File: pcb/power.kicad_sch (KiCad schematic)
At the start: 60 parts, among them J7 1S LiPo, Q1 Q_Dual_NMOS_S1G1S2G2D2D2D1D1, Q2 Q_Dual_NMOS_S1G1S2G2D2D2D1D1, Q3 Q_Dual_NMOS_S1G1S2G2D2D2D1D1, U13 BQ25798, U14 TPS63060, U15 TPS61089

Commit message: add the capacitor the charger's system pin was owed, and take the switch nodes off the top layer
Three things, all of them the charger's own layout list read one item at a time.

C97 is a new part in the drawing. Item one asks for a 0.1uF at the SYS pin on top of the IC, and this
board had one 0.1uF on the system rail with two parts entitled to it -- the charger's SYS pin and the
3.3V converter's input, different pins on different packages millimetres apart. One capacitor cannot
sit on top of both, and the placement pass had to choose, so the charger's was simply missing. Each
pin now has its own, at 1.6mm and 1.5mm.

The switch nodes now leave through a column of vias to the back, which is item two and follows from
item one: holding the capacitors against the package leaves the inductor nowhere near to go. The back
rather than an inner layer on purpose -- the inner layers here are a solid ground plane and the
rails, and a switch node run between them is a capacitor to both along its whole length, against the
same item's instruction to minimize parasitic capacitance from that area to any other trace or plane.
Three vias at the pin and two at the coil, per item six. It works on the buck-boost and not on the
other two: a 0.6mm via wants more room beside a pin than the charger's 0.4mm pitch leaves, and going
smaller would mean a via under the board's own minimum, which is not a trade to make quietly.

And the reservoirs follow the small capacitors in, one per part per rail, which is the rest of item
one and the whole of item five. The battery reservoir went from 14.0mm to 3.2mm and REGN from 8.7 to
2.2mm.

Four faults of my own on the way, each found by measuring rather than by reading the code. Matching a
capacitor to a pin by net alone dragged nine of the processor's and hub's decoupling to the 3.3V
converter's output; it has to be the same sheet. Claiming by PIN let one part take every capacitor on
a rail it has two pins on, so both system-rail capacitors went to th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
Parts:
- added C97: 100n, Capacitor_SMD:C_0402_1005Metric, symbol Device:C_Small
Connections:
- net GND: now also C97.2
- net VSYS: now also C97.1
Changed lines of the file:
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@@
 		(color 0 0 0 0)
 	)
+	(symbol
+		(lib_id "Device:C_Small")
+		(at 114.30 162.56 0)
+		(unit 1)
+		(body_style 1)
+		(exclude_from_sim no)
+		(in_bom yes)
+		(on_board yes)
+		(in_pos_files yes)
+		(dnp no)
+		(property "Reference" "C97"
+			(at 114.30 154.94 0)
+			(show_name no)
+			(do_not_autoplace no)
+			(effects
+				(font
+					(size 1.27 1.27)
+				)
+			)
+		)
+		(property "Value" "100n"
+			(at 114.30 170.18 0)
+			(show_name no)
+			(do_not_autoplace no)
+			(effects
+				(font
+					(size 1.27 1.27)
+				)
+			)
+		)
+		(property "Voltage" "16V"
+			(at 114.30 170.18 0)
+			(hide yes)
+			(show_name no)
+			(do_not_autoplace no)
+			(effects
+				(font
+					(size 1.27 1.27)
+				)
+			)
+		)
+		(property "Dielectric" "X7R"
+			(at 114.30 170.18 0)
+			(hide yes)
+			(show_name no)
+			(do_not_autoplace no)
+			(effects
+				(font
+					(size 1.27 1.27)
+				)
+			)
+		)
+		(property "Footprint" "Capacitor_SMD:C_0402_1005Metric"
+			(at 114.30 162.56 0)
+			(show_name no)
+			(do_not_autoplace no)
+			(effects
+				(font
+					(size 1.27 1.27)
+				)
+			)
+		)
+		(property "Datasheet" ""
+			(at 114.30 162.56 0)
+			(show_name no)
+			(do_not_autoplace no)
+			(effects
+				(font
+					(size 1.27 1.27)
+				)
+			)
+		)
+		(property "Description" ""
+			(at 114.30 162.56 0)
+			(show_name no)
+			(do_not_autoplace no)
+			(effects
+				(font
+					(size 1.27 1.27)
+				)
+			)
+		)
+		(pin "1"
+		)
+		(pin "2"
+		)
+		(instances
+			(project "crossfire"
+				(path "/4c5cdd13-4f54-43b0-affb-0ae4b9a4d279/3a0d800d-f868-47e5-a520-4703480651cc"
+					(reference "C97")
+					(unit 1)
+				)
+			)
+		)
+	)
+	(symbol
+		(lib_id "power:GND")
+		(at 114.30 170.18 0)
+		(unit 1)
+		(body_style 1)
+		(exclude_from_sim no)
+		(in_bom yes)
+		(on_board yes)
+		(in_pos_files yes)
+		(dnp no)
+		(property "Reference" "#PWR119"
+			(at 114.30 163.83 0)
+			(hide yes)
+			(show_name no)
+			(do_not_autoplace no)
+			(effects
+				(font
+					(size 1.27 1.27)
+				)
+			)
+		)
+		(property "Value" "GND"
+			(at 114.30 173.99 0)
+			(show_name no)
+			(do_not_autoplace no)
+			(effects
+				(font
+					(size 1.27 1.27)
+				)
+			)
+		)
+		(property "Footprint" ""
+			(at 114.30 170.18 0)
+			(show_name no)
+			(do_not_autoplace no)
+			(effects
+				(font
+					(size 1.27 1.27)
+				)
+			)
+		)
+		(property "Datasheet" ""
+			(at 114.30 170.18 0)
+			(show_name no)
+			(do_not_autoplace no)
+			(effects
+				(font
+					(size 1.27 1.27)
+				)
+			)
+		)
+		(property "Description" ""
+			(at 114.30 170.18 0)
+			(show_name no)
+			(do_not_autoplace no)
+			(effects
+				(font
+					(size 1.27 1.27)
+				)
+			)
+		)
+		(pin "1"
+		)
+		(instances
+			(project "crossfire"
+				(path "/4c5cdd13-4f54-43b0-affb-0ae4b9a4d279/3a0d800d-f868-47e5-a520-4703480651cc"
+					(reference "#PWR119")
+					(unit 1)
+				)
+			)
+		)
+	)
+	(wire
+		(pts
+			(xy 114.30 160.02) (xy 114.30 157.48)
+		)
+		(stroke
+			(width 0)
+			(type default)
+		)
+	)
+	(wire
+		(pts
+			(xy 114.30 165.10) (xy 114.30 170.18)
+		)
+		(stroke
+			(width 0)
+			(type default)
+		)
+	)
+	(wire
+		(pts
+			(xy 104.14 157.48) (xy 114.30 157.48)
+		)
+		(stroke
+			(width 0)
+			(type default)
+		)
+	)
+	(junction
+		(at 104.14 157.48)
+		(diameter 0)
+		(color 0 0 0 0)
+	)
 )

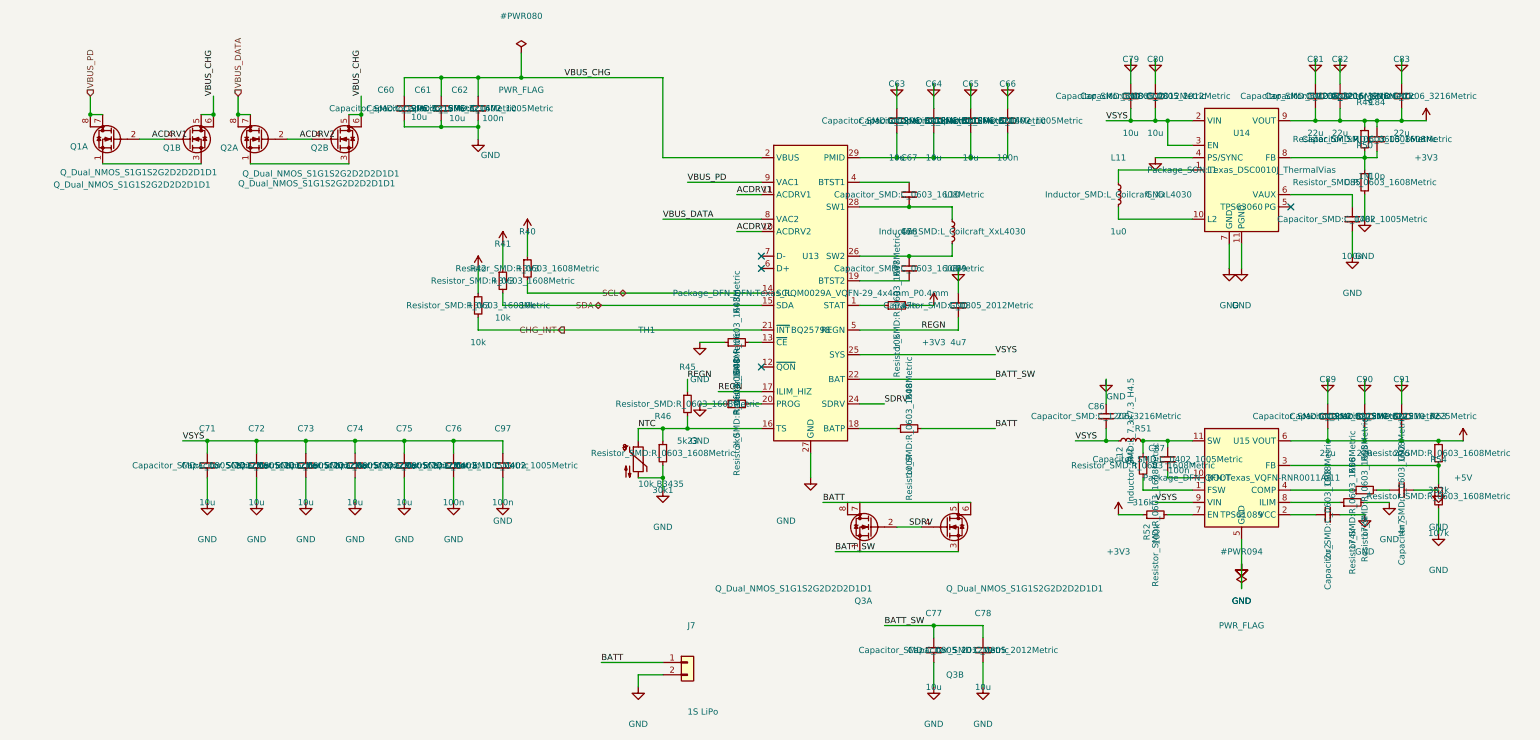
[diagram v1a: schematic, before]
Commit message: checkpoint the battery, PD and radio design as it stood
The last state of the full-featured board before it is reduced to a single
USB-C input: the power block re-placed part by part in order of importance,
the charger's signal pins fanned out, the differential pairs renamed so the
layout tool recognises them, the 3.3 V converter's feedback divider joined
to its pin, the FETs given their part number, and the non-printing fields
hidden on the schematic. The layout is incomplete and is recorded as such.

Co-Authored-By: Claude Fable 5.1 <noreply@anthropic.com>
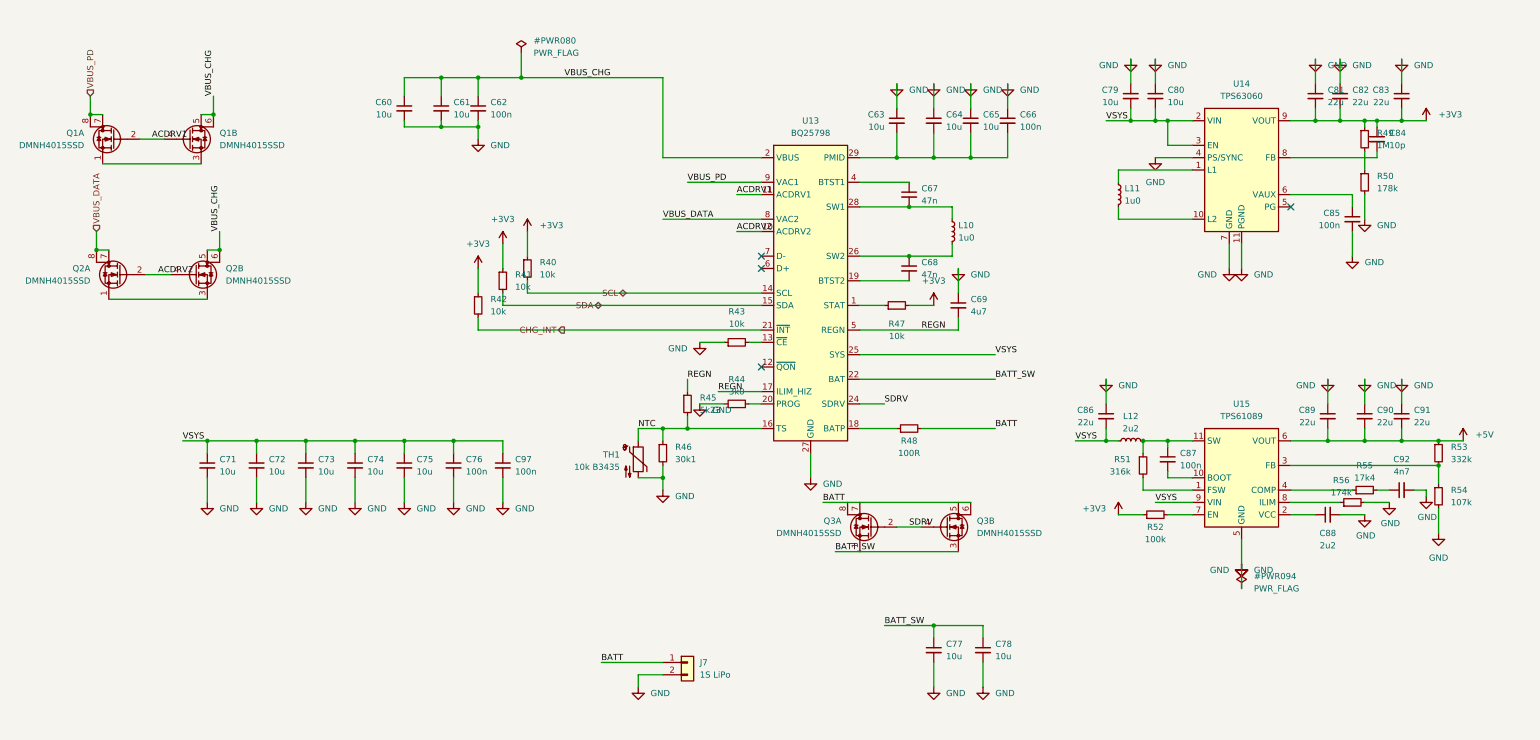
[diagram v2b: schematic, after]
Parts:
- Q1, Q2, Q3: value Q_Dual_NMOS_S1G1S2G2D2D2D1D1 -> DMNH4015SSD
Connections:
- net at R49.2, R50.1: no longer C84.2, U14.8 (FB)
- new net: C84.2, U14.8 (FB)
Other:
- moved on the sheet: Q2A, Q2B

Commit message: reduce the board to a single USB-C input
The PD sink and its connector, the charger and the cell, the input and ship
switches, the 5 V boost, the 3.3 V buck-boost and the radio come off. The
one remaining USB-C receptacle carries data to the hardware controller and
its VBUS is the 5 V rail: straight to the four port switches, and to a
fixed 3.3 V buck (AP63203) for everything else.

The two CC pins are read by ADC inputs through 10k into 100n, in series so
the 5.1k termination is not loaded, so firmware can tell a 3 A source from
a 1.5 A one from a default port and power the ports to fit.

Schematic: radio and upstream_power sheets removed, power sheet redrawn,
seven MCU pins freed and two taken. Board: 61 footprints and 514 tracks and
vias removed, survivors re-netted from the netlist, new parts loaded but
not placed. The layout is to be redone and the design document says so; it
is rewritten for this design, with what the single input gives up stated.

Co-Authored-By: Claude Fable 5.1 <noreply@anthropic.com>
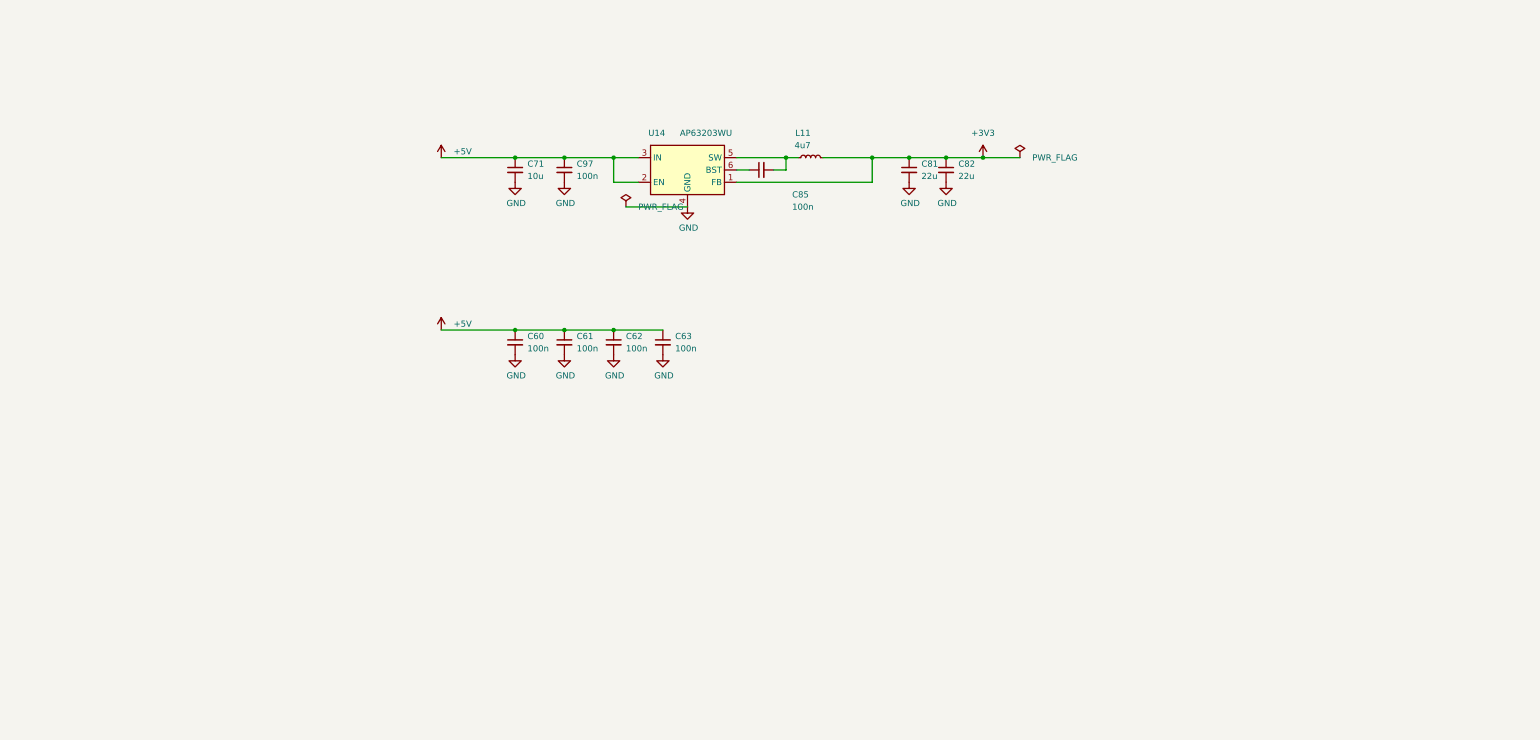
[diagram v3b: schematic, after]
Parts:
- removed C64, C65: 10u, Capacitor_SMD:C_1206_3216Metric, symbol Device:C_Small
- removed C66, C76, C87: 100n, Capacitor_SMD:C_0402_1005Metric, symbol Device:C_Small
- removed C67, C68: 47n, Capacitor_SMD:C_0603_1608Metric, symbol Device:C_Small
- removed C69: 4u7, Capacitor_SMD:C_0805_2012Metric, symbol Device:C_Small
- removed C72, C73, C74, C75, C77, C78, C79, C80: 10u, Capacitor_SMD:C_0805_2012Metric, symbol Device:C_Small
- removed C83, C86: 22u, Capacitor_SMD:C_1206_3216Metric, symbol Device:C_Small
- removed C84: 10p, Capacitor_SMD:C_0603_1608Metric, symbol Device:C_Small
- removed C88: 2u2, Capacitor_SMD:C_0603_1608Metric, symbol Device:C_Small
- removed C89, C90, C91: 22u, Capacitor_SMD:C_1210_3225Metric, symbol Device:C_Small
- removed C92: 4n7, Capacitor_SMD:C_0603_1608Metric, symbol Device:C_Small
- removed J7: 1S LiPo, Connector_JST:JST_PH_B2B-PH-K_1x02_P2.00mm_Vertical, symbol Connector_Generic:Conn_01x02
- removed L10: 1u0, Inductor_SMD:L_Coilcraft_XxL4030, symbol Device:L_Small
- removed L12: 2u2, Inductor_SMD:L_7.3x7.3_H4.5, symbol Device:L_Small
- removed Q1, Q2, Q3: DMNH4015SSD, Package_SO:SOIC-8_3.9x4.9mm_P1.27mm, symbol Transistor_FET:Q_Dual_NMOS_S1G1S2G2D2D2D1D1
- removed R40, R41, R42, R43, R47: 10k, Resistor_SMD:R_0603_1608Metric, symbol Device:R_Small
- removed R44: 3k0, Resistor_SMD:R_0603_1608Metric, symbol Device:R_Small
- removed R45: 5k23, Resistor_SMD:R_0603_1608Metric, symbol Device:R_Small
- removed R46: 30k1, Resistor_SMD:R_0603_1608Metric, symbol Device:R_Small
- removed R48: 100R, Resistor_SMD:R_0603_1608Metric, symbol Device:R_Small
- removed R49: 1M, Resistor_SMD:R_0603_1608Metric, symbol Device:R_Small
- removed R50: 178k, Resistor_SMD:R_0603_1608Metric, symbol Device:R_Small
- removed R51: 316k, Resistor_SMD:R_0603_1608Metric, symbol Device:R_Small
- removed R52: 100k, Resistor_SMD:R_0603_1608Metric, symbol Device:R_Small
- removed R53: 332k, Resistor_SMD:R_0603_1608Metric, symbol Device:R_Small
- removed R54: 107k, Resistor_SMD:R_0603_1608Metric, symbol Device:R_Small
- removed R55: 17k4, Resistor_SMD:R_0603_1608Metric, symbol Device:R_Small
- removed R56: 174k, Resistor_SMD:R_0603_1608Metric, symbol Device:R_Small
- removed TH1: 10k B3435, Resistor_SMD:R_0603_1608Metric, symbol Device:Thermistor_NTC
- removed U13: BQ25798, Package_DFN_QFN:Texas_RQM0029A_VQFN-29_4x4mm_P0.4mm, symbol Battery_Management:BQ25798
- removed U15: TPS61089, Package_DFN_QFN:Texas_VQFN-RNR0011A-11, symbol Regulator_Switching:TPS61089
- C60, C61, C63: value 10u -> 100n; footprint Capacitor_SMD:C_1206_3216Metric -> Capacitor_SMD:C_0402_1005Metric
- C71, C97: Voltage 16V -> 25V
- L11: value 1u0 -> 4u7; Isat 7.6A @20% -> 2A min; MPN Coilcraft XGL4030-102MEC -> 4.7 uH, 4 mm shielded; part to confirm
- U14: value TPS63060 -> AP63203WU; footprint Package_SON:Texas_DSC0010J_ThermalVias -> Package_TO_SOT_SMD:TSOT-23-6; symbol Regulator_Switching:TPS63060 -> Regulator_Switching:AP63203WU
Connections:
- net VBUS_CHG is gone; now on net +5V: C60.1, C61.1, C62.1
- net VSYS is gone; now on net +5V: C71.1, C97.1, U14.2 (EN), U14.3 (IN)
- net +3V3: now also C81.1, C82.1, L11.2, U14.1 (FB); no longer C81.2, C82.2, U14.9 (VOUT)
- net +5V: now also C63.1
- net GND: now also C63.2, C81.2, C82.2; no longer C63.1, C81.1, C82.1, C85.2, U14.11 (PGND), U14.7 (GND)
- net at L11.1: now also C85.2, U14.5 (SW); no longer U14.1 (L1)
- no-connect marks 4 -> 0
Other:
- moved on the sheet: C71, C81, C82, C85, C97, L11

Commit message: take the processor's regulator parts from the vendor's reference design
4.7 uF in 0402 on VREG_VIN and on the core rail, where this board had 10 uF
and 4.7 uF in 0805, and a 33 ohm / 4.7 uF filter on VREG_AVDD, which it
did not have at all. The crystal's load capacitors go to 0402 and the
3.3 V buck's capacitors to 0603. Footprints are swapped on the board in
place so the layout stands; R5 and C16 are parked outside the left edge.

Co-Authored-By: Claude Fable 5.1 <noreply@anthropic.com>
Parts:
- C71: footprint Capacitor_SMD:C_0805_2012Metric -> Capacitor_SMD:C_0603_1608Metric; Dielectric X7R -> X5R; Voltage 25V -> 10V
- C81, C82: footprint Capacitor_SMD:C_1206_3216Metric -> Capacitor_SMD:C_0603_1608Metric; Dielectric X7R -> X5R; Voltage 16V -> 6.3V
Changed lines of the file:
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@@
 			)
 		)
-		(property "Footprint" "Capacitor_SMD:C_1206_3216Metric"
+		(property "Footprint" "Capacitor_SMD:C_0603_1608Metric"
 			(at 205.74 101.6 0)
 			(hide yes)
@@
 			)
 		)
-		(property "Voltage" "16V"
+		(property "Voltage" "6.3V"
 			(at 205.74 109.22 0)
 			(hide yes)
@@
 			)
 		)
-		(property "Dielectric" "X7R"
+		(property "Dielectric" "X5R"
 			(at 205.74 109.22 0)
 			(hide yes)
@@
 			)
 		)
-		(property "Footprint" "Capacitor_SMD:C_0805_2012Metric"
+		(property "Footprint" "Capacitor_SMD:C_0603_1608Metric"
 			(at 116.84 101.6 0)
 			(hide yes)
@@
 			)
 		)
-		(property "Voltage" "25V"
+		(property "Voltage" "10V"
 			(at 116.84 109.22 0)
 			(hide yes)
@@
 			)
 		)
-		(property "Dielectric" "X7R"
+		(property "Dielectric" "X5R"
 			(at 116.84 109.22 0)
 			(hide yes)
@@
 			)
 		)
-		(property "Footprint" "Capacitor_SMD:C_1206_3216Metric"
+		(property "Footprint" "Capacitor_SMD:C_0603_1608Metric"
 			(at 198.12 101.6 0)
 			(hide yes)
@@
 			)
 		)
-		(property "Voltage" "16V"
+		(property "Voltage" "6.3V"
 			(at 198.12 109.22 0)
 			(hide yes)
@@
 			)
 		)
-		(property "Dielectric" "X7R"
+		(property "Dielectric" "X5R"
 			(at 198.12 109.22 0)
 			(hide yes)
